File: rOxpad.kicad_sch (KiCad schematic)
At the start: 22 parts, among them SW1 SW_Push, U1 ATmega32U4-A, Y1 16MHz

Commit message: Applied footprints!
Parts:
- SW1: footprint (none) -> random-keyboard-parts:SKQG-1155865
- USB1: footprint (none) -> random-keyboard-parts:Molex-0548190589
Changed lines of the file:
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@@
       (effects (font (size 1.524 1.524)))
     )
-    (property "Footprint" "" (id 2) (at 154.94 39.37 0)
+    (property "Footprint" "random-keyboard-parts:Molex-0548190589" (id 2) (at 154.94 39.37 0)
       (effects (font (size 1.524 1.524)) hide)
     )
@@
     (property "Reference" "SW1" (id 0) (at 64.77 29.21 0))
     (property "Value" "SW_Push" (id 1) (at 64.77 31.75 0))
-    (property "Footprint" "" (id 2) (at 64.77 31.75 0)
+    (property "Footprint" "random-keyboard-parts:SKQG-1155865" (id 2) (at 64.77 31.75 0)
       (effects (font (size 1.27 1.27)) hide)
     )
@@
     )
     (path "/eba00549-67ff-4f83-9a55-44db8913d52d"
-      (reference "SW1") (unit 1) (value "SW_Push") (footprint "")
+      (reference "SW1") (unit 1) (value "SW_Push") (footprint "random-keyboard-parts:SKQG-1155865")
     )
     (path "/74076de0-c6fa-447a-ba76-bbb1ca74e2e2"
@@
     )
     (path "/a3373ae3-0597-4f5e-81ea-f528b682f403"
-      (reference "USB1") (unit 1) (value "Molex-0548190589") (footprint "")
+      (reference "USB1") (unit 1) (value "Molex-0548190589") (footprint "random-keyboard-parts:Molex-0548190589")
     )
     (path "/6ae1b276-d408-4f41-881b-c66f44d934a7"

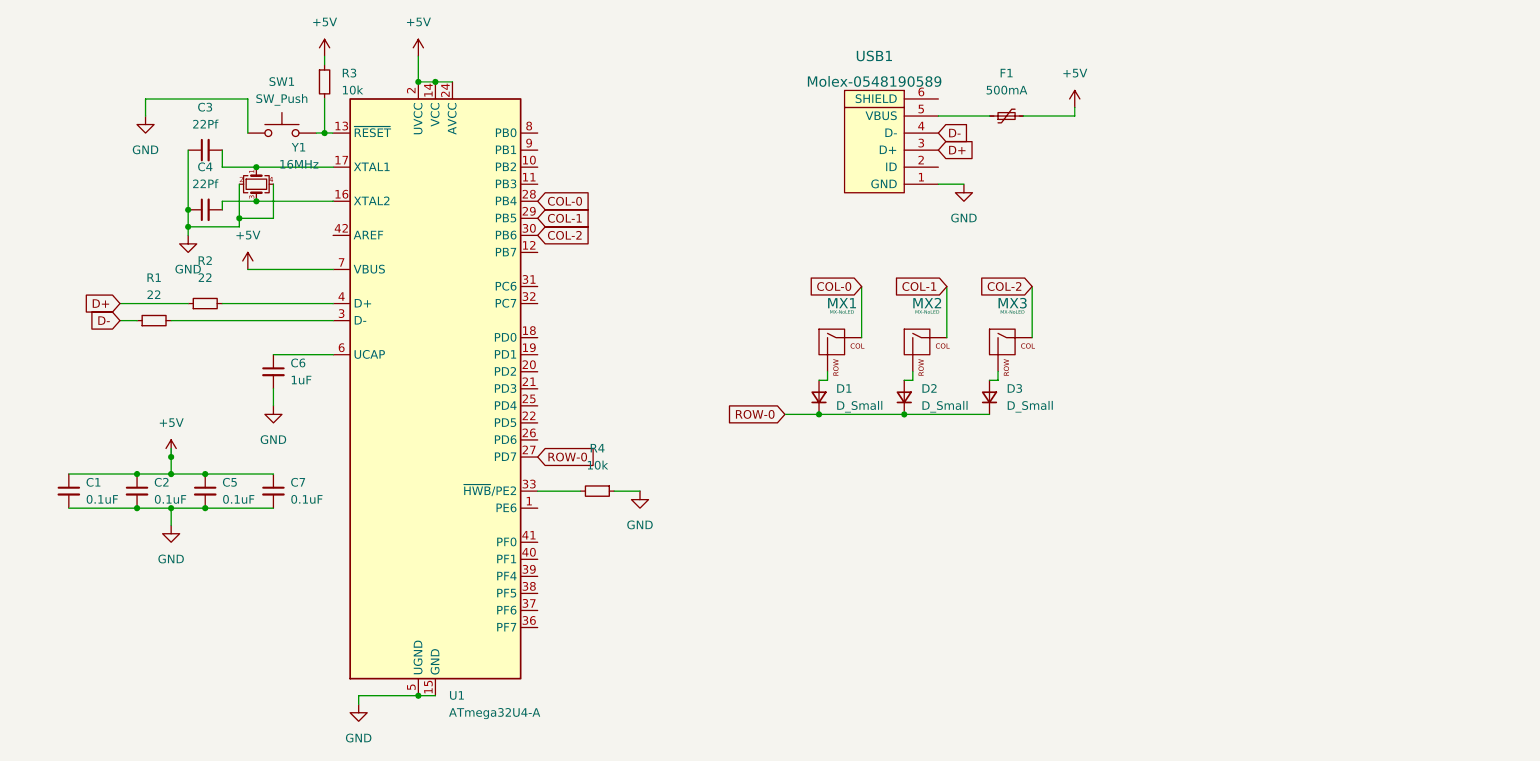
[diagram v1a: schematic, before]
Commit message: started redesigning the schematic
didn't like the result lol
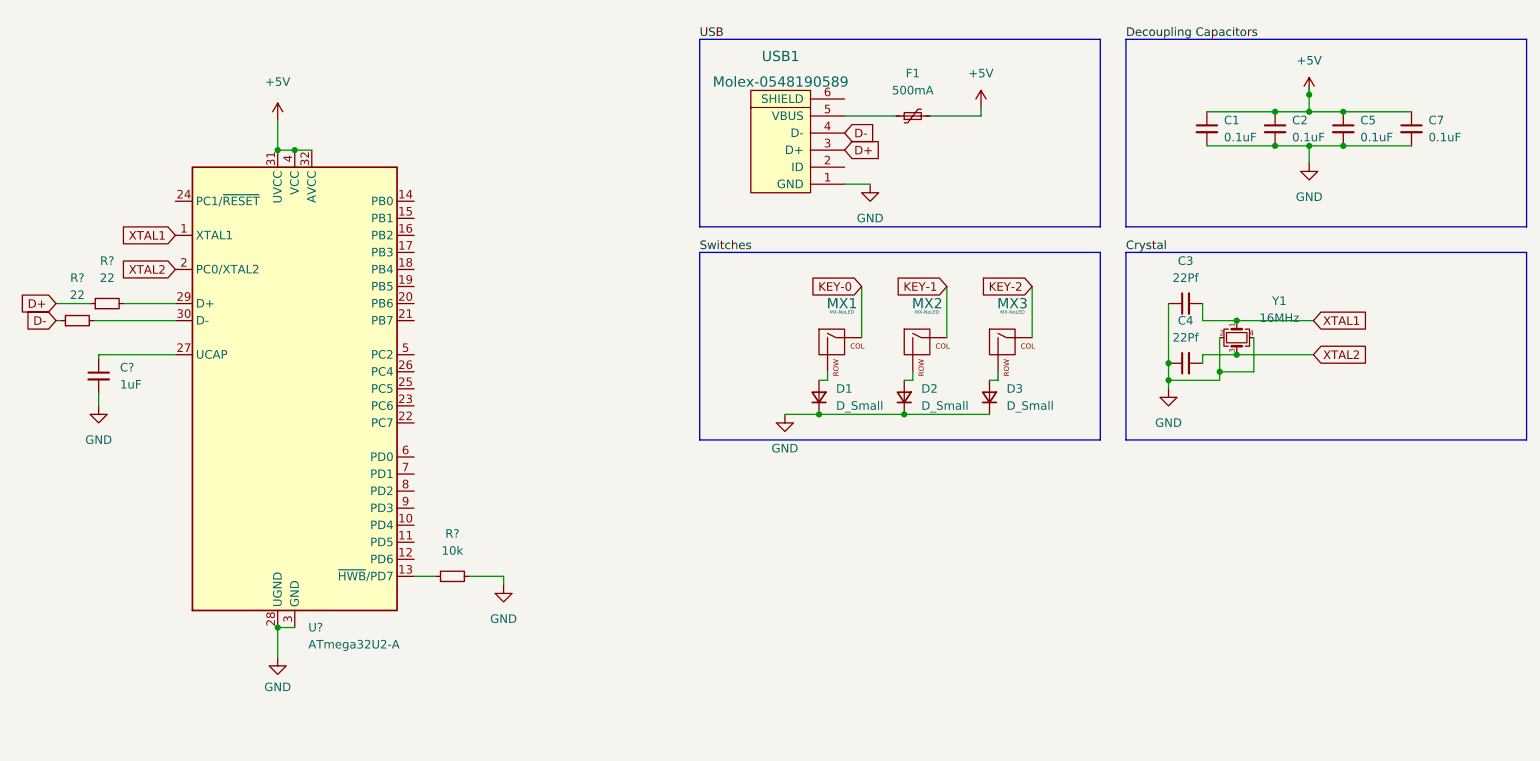
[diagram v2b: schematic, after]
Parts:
- removed C6: 1uF, Capacitor_SMD:C_0805_2012Metric, symbol Device:C_Small
- removed R1, R2: 22, Resistor_SMD:R_0805_2012Metric, symbol Device:R_Small
- removed R3, R4: 10k, Resistor_SMD:R_0805_2012Metric, symbol Device:R_Small
- removed SW1: SW_Push, random-keyboard-parts:SKQG-1155865, symbol Switch:SW_Push
- removed U1: ATmega32U4-A, Package_QFP:TQFP-44_10x10mm_P0.8mm, symbol MCU_Microchip_ATmega:ATmega32U4-A
- added C?: 1uF, symbol Device:C_Small
- added R? (x2): 22, symbol Device:R_Small
- added R?: 10k, symbol Device:R_Small
- added U?: ATmega32U2-A, Package_QFP:TQFP-32_7x7mm_P0.8mm, symbol MCU_Microchip_ATmega:ATmega32U2-A
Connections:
- net ROW-0 is gone; now on net GND: D1.1 (K), D2.1 (K), D3.1 (K)
- net +5V: now also U?.31 (UVCC), U?.32 (AVCC), U?.4 (VCC)
- net D+: now also R?.1
- net D-: now also R?.1
- net GND: now also C?.2, R?.2, U?.28 (UGND), U?.3 (GND)
- net XTAL2: now reaches C4.2, Y1.3
- net XTAL2: now also U?.2 (PC0/XTAL2)
- net XTAL1: now reaches C3.2, Y1.1
- net XTAL1: now also U?.1 (XTAL1)
- net COL-0 renamed KEY-0
- net COL-1 renamed KEY-1
- net COL-2 renamed KEY-2
- new net: R?.2, U?.29 (D+)
- new net: R?.1, U?.13 (~{HWB}/PD7)
- new net: C?.1, U?.27 (UCAP)
- new net: R?.2, U?.30 (D-)
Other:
- moved on the sheet: C1, C2, C3, C4, C5, C7, F1, USB1, Y1

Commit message: add another submodule, and continue with schem v2
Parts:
- removed F1: 500mA, Fuse:Fuse_1206_3216Metric, symbol Device:Polyfuse_Small
- removed USB1: Molex-0548190589, random-keyboard-parts:Molex-0548190589, symbol random-keyboard-parts:Molex-0548190589
- added F?: Polyfuse_Small, symbol Device:Polyfuse_Small
- added R? (x2): 5.1k, symbol Device:R_Small
- added R?: 10k, symbol Device:R_Small
- added SW?: SW_Push, symbol Switch:SW_Push
- added USB?: HRO-TYPE-C-31-M-12, symbol Type-C:HRO-TYPE-C-31-M-12
- C?: renamed from C7; value 0.1uF -> 10uF
- renumbered C4 to C?, C1 to C?, C5 to C?, C2 to C?, C3 to C?, D1 to D?, D3 to D?, D2 to D?, MX3 to MX?, MX1 to MX?, MX2 to MX?, Y1 to Y?
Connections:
- net +5V: now also F?.2, R?.1
- net D+: now also USB?.6 (DP1), USB?.8 (DP2)
- net D-: now also USB?.5 (DN2), USB?.7 (DN1)
- net GND: now also R?.2, R?.2, SW?.1, USB?.1 (GND), USB?.12 (GND), USB?.13 (SHIELD)
- net at U?.24 (PC1/~{RESET}): now also R?.2, SW?.2
- new net: R?.1, USB?.10 (CC2)
- new net: R?.1, USB?.4 (CC1)
- new net VCC: F?.1, USB?.11 (VBUS), USB?.2 (VBUS)
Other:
- moved on the sheet: C?, D?, MX?, Y?

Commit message: I think it's finished wohoo
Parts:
- removed U?: ATmega32U2-A, Package_QFP:TQFP-32_7x7mm_P0.8mm, symbol MCU_Microchip_ATmega:ATmega32U2-A
- added U1: ATmega16U2-A, Package_QFP:TQFP-32_7x7mm_P0.8mm, symbol MCU_Microchip_ATmega:ATmega16U2-A
- added U2: PRTR5V0U2X, random-keyboard-parts:SOT143B, symbol random-keyboard-parts:PRTR5V0U2X
- C1: renamed from C?; footprint (none) -> Capacitor_SMD:C_0805_2012Metric_Pad1.18x1.45mm_HandSolder
- C2, C3, C4, C5, C6, C7: renamed from C?; footprint Capacitor_SMD:C_0805_2012Metric -> Capacitor_SMD:C_0805_2012Metric_Pad1.18x1.45mm_HandSolder
- F1: renamed from F?; footprint (none) -> Fuse:Fuse_1206_3216Metric_Pad1.42x1.75mm_HandSolder
- MX1, MX2, MX3: renamed from MX?; footprint MX_Alps_Hybrid:MX-1U-NoLED -> MX_Only:MXOnly-1U-Hotswap
- R1, R2, R3, R4, R5, R6: renamed from R?; footprint (none) -> Resistor_SMD:R_0805_2012Metric_Pad1.20x1.40mm_HandSolder
- SW1: renamed from SW?; footprint (none) -> random-keyboard-parts:SKQG-1155865
- USB1: renamed from USB?; footprint (none) -> Type-C:HRO-TYPE-C-31-M-12-HandSoldering
- gave numbers to parts that had none: 4
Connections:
- net +5V: now also U1.31 (UVCC), U1.32 (AVCC), U1.4 (VCC)
- net D+: now also U2.2 (IO1)
- net D-: now also U2.3 (IO2)
- net GND: now also U1.28 (UGND), U1.3 (GND), U2.1 (GND)
- net KEY-0: now also U1.19 (PB5)
- net KEY-1: now also U1.20 (PB6)
- net KEY-2: now also U1.21 (PB7)
- net VCC: now also U2.4 (VCC)
- net XTAL1: now also U1.1 (XTAL1)
- net XTAL2: now also U1.2 (PC0/XTAL2)
- net at R2.2: now also U1.29 (D+)
- net at R4.1: now also U1.13 (~{HWB}/PD7)
- net at R3.2, SW1.2: now also U1.24 (PC1/~{RESET})
- net at C1.1: now also U1.27 (UCAP)
- net at R1.2: now also U1.30 (D-)
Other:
- moved on the sheet: D1, D2, D3, F1, MX1, MX2, MX3, R5, R6, USB1

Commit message: Made some changes so it's doesn't explode
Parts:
- removed C6: 0.1uF, Capacitor_SMD:C_0805_2012Metric_Pad1.18x1.45mm_HandSolder, symbol Device:C_Small
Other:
- moved on the sheet: C7
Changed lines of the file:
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@@
   (junction (at 217.805 38.735) (diameter 0) (color 0 0 0 0)
   )
-  (junction (at 222.885 33.655) (diameter 0) (color 0 0 0 0)
-  )
   (junction (at 217.805 31.115) (diameter 0) (color 0 0 0 0)
   )
@@
   (junction (at 160.02 38.1) (diameter 0) (color 0 0 0 0)
   )
-  (junction (at 222.885 38.735) (diameter 0) (color 0 0 0 0)
-  )
   (junction (at 139.065 33.02) (diameter 0) (color 0 0 0 0)
   )
@@
     (stroke (width 0) (type default) (color 0 0 0 0))
   )
-  (wire (pts (xy 217.805 33.655) (xy 222.885 33.655))
-    (stroke (width 0) (type default) (color 0 0 0 0))
-  )
   (wire (pts (xy 132.08 38.1) (xy 146.05 38.1))
     (stroke (width 0) (type default) (color 0 0 0 0))
@@
     (stroke (width 0) (type default) (color 0 0 0 0))
   )
-  (wire (pts (xy 217.805 38.735) (xy 222.885 38.735))
+  (wire (pts (xy 217.805 38.735) (xy 224.155 38.735))
     (stroke (width 0) (type default) (color 0 0 0 0))
   )
@@
     (stroke (width 0) (type default) (color 0 0 0 0))
   )
-  (wire (pts (xy 222.885 33.655) (xy 233.045 33.655))
+  (wire (pts (xy 217.805 33.655) (xy 224.155 33.655))
     (stroke (width 0) (type default) (color 0 0 0 0))
   )
@@
   )
   (wire (pts (xy 204.47 85.09) (xy 209.55 85.09))
-    (stroke (width 0) (type default) (color 0 0 0 0))
-  )
-  (wire (pts (xy 222.885 38.735) (xy 233.045 38.735))
     (stroke (width 0) (type default) (color 0 0 0 0))
   )
@@
     (pin "2")
   )
-  (symbol (lib_id "Device:C_Small") (at 222.885 36.195 0) (unit 1)
-    (in_bom yes) (on_board yes) (fields_autoplaced)
-    (property "Reference" "C6" (id 0) (at 226.06 34.9312 0)
-      (effects (font (size 1.27 1.27)) (justify left))
-    )
-    (property "Value" "0.1uF" (id 1) (at 226.06 37.4712 0)
-      (effects (font (size 1.27 1.27)) (justify left))
-    )
-    (property "Footprint" "Capacitor_SMD:C_0805_2012Metric_Pad1.18x1.45mm_HandSolder" (id 2) (at 222.885 36.195 0)
-      (effects (font (size 1.27 1.27)) hide)
-    )
-    (property "Datasheet" "~" (id 3) (at 222.885 36.195 0)
-      (effects (font (size 1.27 1.27)) hide)
-    )
-    (pin "1")
-    (pin "2")
-  )
   (symbol (lib_id "Device:Crystal_GND24_Small") (at 207.01 80.01 270) (unit 1)
     (in_bom yes) (on_board yes) (fields_autoplaced)
@@
     (pin "2")
   )
-  (symbol (lib_id "Device:C_Small") (at 233.045 36.195 0) (unit 1)
-    (in_bom yes) (on_board yes) (fields_autoplaced)
-    (property "Reference" "C7" (id 0) (at 236.22 34.9312 0)
+  (symbol (lib_id "Device:C_Small") (at 224.155 36.195 0) (unit 1)
+    (in_bom yes) (on_board yes) (fields_autoplaced)
+    (property "Reference" "C7" (id 0) (at 227.33 34.9312 0)
       (effects (font (size 1.27 1.27)) (justify left))
     )
-    (property "Value" "10uF" (id 1) (at 236.22 37.4712 0)
+    (property "Value" "10uF" (id 1) (at 227.33 37.4712 0)
       (effects (font (size 1.27 1.27)) (justify left))
     )
-    (property "Footprint" "Capacitor_SMD:C_0805_2012Metric_Pad1.18x1.45mm_HandSolder" (id 2) (at 233.045 36.195 0)
-      (effects (font (size 1.27 1.27)) hide)
-    )
-    (property "Datasheet" "~" (id 3) (at 233.045 36.195 0)
+    (property "Footprint" "Capacitor_SMD:C_0805_2012Metric_Pad1.18x1.45mm_HandSolder" (id 2) (at 224.155 36.195 0)
+      (effects (font (size 1.27 1.27)) hide)
+    )
+    (property "Datasheet" "~" (id 3) (at 224.155 36.195 0)
       (effects (font (size 1.27 1.27)) hide)
     )
@@
       (reference "C5") (unit 1) (value "0.1uF") (footprint "Capacitor_SMD:C_0805_2012Metric_Pad1.18x1.45mm_HandSolder")
     )
-    (path "/670519af-e509-43bc-afb7-fd0ca0854ce9"
-      (reference "C6") (unit 1) (value "0.1uF") (footprint "Capacitor_SMD:C_0805_2012Metric_Pad1.18x1.45mm_HandSolder")
-    )
     (path "/ad340931-b8d0-475b-8b44-eac6bba29efa"

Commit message: Changed switch footprint (still same connections)
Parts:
- MX1, MX2, MX3: footprint MX_Only:MXOnly-1U-Hotswap -> marbastlib-mx:SW_MX_HS_1u
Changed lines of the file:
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@@
       (effects (font (size 0.508 0.508)))
     )
-    (property "Footprint" "MX_Only:MXOnly-1U-Hotswap" (id 2) (at 156.21 84.455 0)
+    (property "Footprint" "marbastlib-mx:SW_MX_HS_1u" (id 2) (at 156.21 84.455 0)
       (effects (font (size 1.524 1.524)) hide)
     )
@@
       (effects (font (size 0.508 0.508)))
     )
-    (property "Footprint" "MX_Only:MXOnly-1U-Hotswap" (id 2) (at 130.81 84.455 0)
+    (property "Footprint" "marbastlib-mx:SW_MX_HS_1u" (id 2) (at 130.81 84.455 0)
       (effects (font (size 1.524 1.524)) hide)
     )
@@
       (effects (font (size 0.508 0.508)))
     )
-    (property "Footprint" "MX_Only:MXOnly-1U-Hotswap" (id 2) (at 143.51 84.455 0)
+    (property "Footprint" "marbastlib-mx:SW_MX_HS_1u" (id 2) (at 143.51 84.455 0)
       (effects (font (size 1.524 1.524)) hide)
     )
@@
     )
     (path "/782fd8a6-8a59-4468-aed8-e7f14a0f2386"
-      (reference "MX1") (unit 1) (value "MX-NoLED") (footprint "MX_Only:MXOnly-1U-Hotswap")
+      (reference "MX1") (unit 1) (value "MX-NoLED") (footprint "marbastlib-mx:SW_MX_HS_1u")
     )
     (path "/f84ce8da-348a-401b-baf3-2d32c1b70a34"
-      (reference "MX2") (unit 1) (value "MX-NoLED") (footprint "MX_Only:MXOnly-1U-Hotswap")
+      (reference "MX2") (unit 1) (value "MX-NoLED") (footprint "marbastlib-mx:SW_MX_HS_1u")
     )
     (path "/514e299f-6221-4a3d-8063-7d0f70478444"
-      (reference "MX3") (unit 1) (value "MX-NoLED") (footprint "MX_Only:MXOnly-1U-Hotswap")
+      (reference "MX3") (unit 1) (value "MX-NoLED") (footprint "marbastlib-mx:SW_MX_HS_1u")
     )
     (path "/a68f94c7-99b9-45a8-a7ce-5c56335f37d0"

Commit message: Main board wiring finished (i hope)
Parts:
- USB1: footprint Type-C:HRO-TYPE-C-31-M-12-HandSoldering -> Connector_USB:USB_C_Receptacle_HRO_TYPE-C-31-M-12
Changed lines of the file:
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@@
       (effects (font (size 1.524 1.524)))
     )
-    (property "Footprint" "Type-C:HRO-TYPE-C-31-M-12-HandSoldering" (id 2) (at 129.54 44.45 0)
+    (property "Footprint" "Connector_USB:USB_C_Receptacle_HRO_TYPE-C-31-M-12" (id 2) (at 129.54 44.45 0)
       (effects (font (size 1.524 1.524)) hide)
     )
@@
     )
     (path "/2762ddf1-ec11-44d9-b2f7-0fe42b7f916e"
-      (reference "USB1") (unit 1) (value "HRO-TYPE-C-31-M-12") (footprint "Type-C:HRO-TYPE-C-31-M-12-HandSoldering")
+      (reference "USB1") (unit 1) (value "HRO-TYPE-C-31-M-12") (footprint "Connector_USB:USB_C_Receptacle_HRO_TYPE-C-31-M-12")
     )
     (path "/6ae1b276-d408-4f41-881b-c66f44d934a7"
